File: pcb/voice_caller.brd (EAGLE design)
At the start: 52.4 x 59.1 mm, 44 parts, among them IC1 PRO_MICRO, IC2 LM386M-1, IC3 78L12SMD, K1 TQ2SA-L2-5V, U1 25F32006WSOI

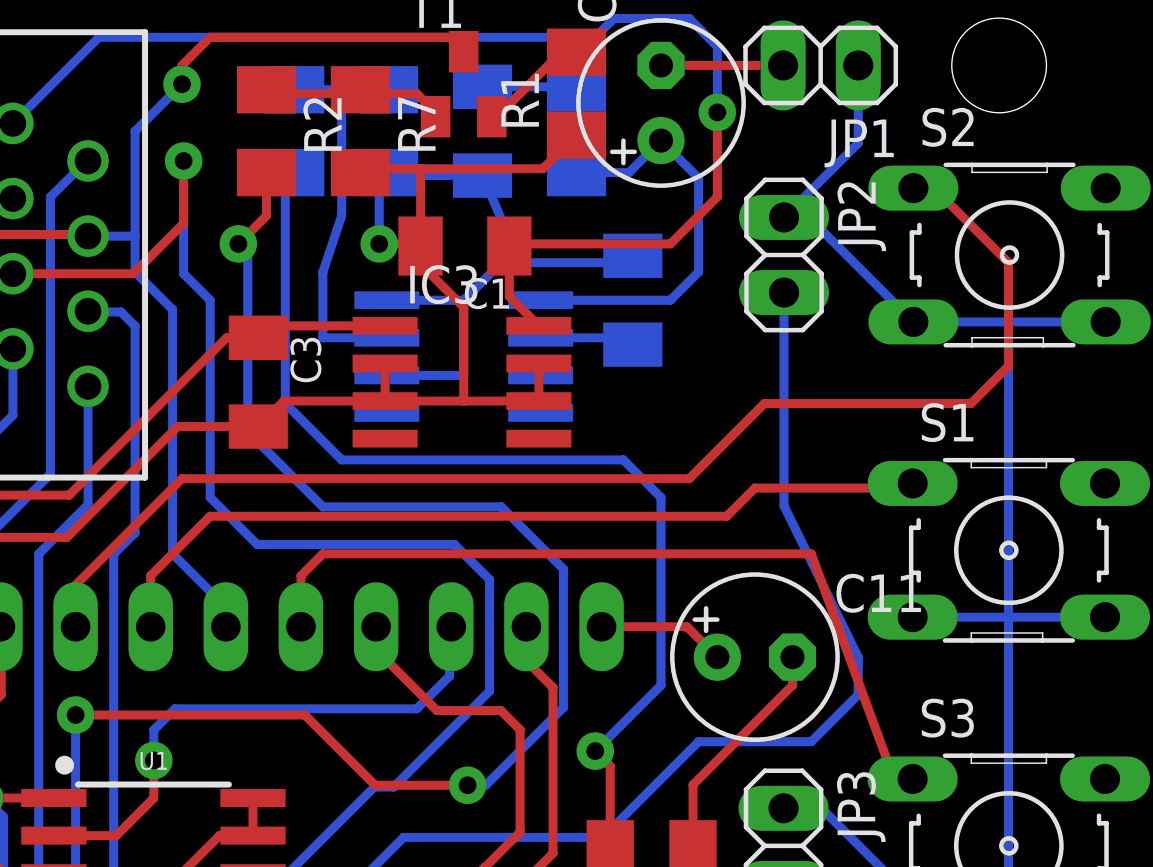
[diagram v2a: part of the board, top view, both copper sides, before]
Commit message: Bypass capacitor added for LM386.
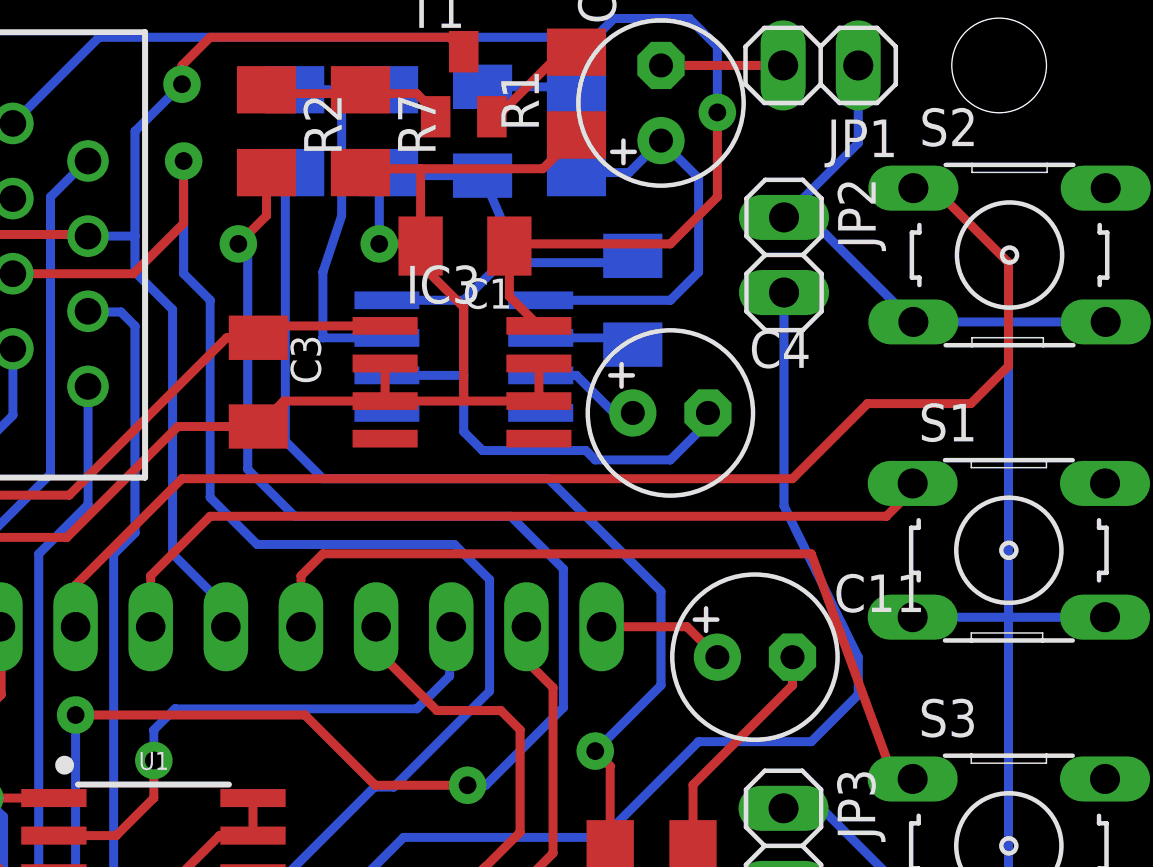
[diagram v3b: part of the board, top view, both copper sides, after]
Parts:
- added C4: (no value), rcl:E2,5-6
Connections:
- new net N$7: C4.+, IC2.7
- net GND: now also C4.-
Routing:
- net GND: track 301.6 -> 313.0 mm
- net N$7: track 0.00 -> 3.64 mm
- net AUDIO: track 49.1 -> 48.0 mm
- net PTT_SW: track 57.4 -> 58.1 mm
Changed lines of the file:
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@@
 <element name="R16" library="rcl" package="M1206" value="220" x="35.2425" y="59.3725" rot="MR90"/>
 <element name="C11" library="rcl" package="E2,5-6" value="" x="47.625" y="41.5925"/>
+<element name="C4" library="rcl" package="E2,5-6" value="" x="44.7675" y="49.8475"/>
 </elements>
 <signals>
@@
 <wire x1="35.2425" y1="57.9725" x2="34.925" y2="57.655" width="0.3048" layer="16"/>
 <wire x1="34.925" y1="57.655" x2="34.925" y2="55.5625" width="0.3048" layer="16"/>
+<contactref element="C4" pad="-"/>
+<wire x1="46.0375" y1="49.8475" x2="46.0375" y2="49.53" width="0.3048" layer="16"/>
+<wire x1="46.0375" y1="49.53" x2="44.7675" y2="48.26" width="0.3048" layer="16"/>
+<wire x1="44.7675" y1="48.26" x2="42.2275" y2="48.26" width="0.3048" layer="16"/>
+<wire x1="42.2275" y1="48.26" x2="41.91" y2="48.5775" width="0.3048" layer="16"/>
+<wire x1="41.91" y1="48.5775" x2="38.4175" y2="48.5775" width="0.3048" layer="16"/>
+<wire x1="38.4175" y1="48.5775" x2="37.7825" y2="49.2125" width="0.3048" layer="16"/>
+<wire x1="37.7825" y1="49.2125" x2="37.7825" y2="51.1175" width="0.3048" layer="16"/>
 </signal>
 <signal name="MOSI">
@@
 <wire x1="44.7675" y1="23.65375" x2="43.65625" y2="22.5425" width="0.3048" layer="1"/>
 <contactref element="R15" pad="2"/>
-<wire x1="43.18" y1="48.26" x2="44.45" y2="46.99" width="0.3048" layer="16"/>
-<wire x1="44.45" y1="46.99" x2="44.45" y2="40.64" width="0.3048" layer="16"/>
+<wire x1="40.64" y1="47.625" x2="44.45" y2="43.815" width="0.3048" layer="16"/>
+<wire x1="44.45" y1="43.815" x2="44.45" y2="40.64" width="0.3048" layer="16"/>
 <wire x1="44.45" y1="40.64" x2="42.2275" y2="38.4175" width="0.3048" layer="16"/>
 <via x="42.2275" y="38.4175" extent="1-16" drill="0.6" diameter="1.27" shape="square"/>
 <wire x1="42.2275" y1="38.4175" x2="42.7325" y2="37.9125" width="0.3048" layer="1"/>
 <wire x1="42.7325" y1="37.9125" x2="42.7325" y2="35.08375" width="0.3048" layer="1"/>
-<wire x1="43.18" y1="48.26" x2="33.655" y2="48.26" width="0.3048" layer="16"/>
-<wire x1="33.655" y1="48.26" x2="31.75" y2="50.165" width="0.3048" layer="16"/>
-<wire x1="31.75" y1="50.165" x2="31.75" y2="57.655" width="0.3048" layer="16"/>
+<wire x1="40.64" y1="47.625" x2="33.02" y2="47.625" width="0.3048" layer="16"/>
+<wire x1="33.02" y1="47.625" x2="31.75" y2="48.895" width="0.3048" layer="16"/>
+<wire x1="31.75" y1="48.895" x2="31.75" y2="57.655" width="0.3048" layer="16"/>
 <wire x1="31.75" y1="57.655" x2="32.0675" y2="57.9725" width="0.3048" layer="16"/>
 </signal>
@@
 <signal name="BUTTON2">
 <contactref element="S1" pad="1"/>
-<wire x1="29.21" y1="46.355" x2="46.6725" y2="46.355" width="0.3048" layer="1"/>
-<wire x1="46.6725" y1="46.355" x2="47.625" y2="47.3075" width="0.3048" layer="1"/>
-<wire x1="47.625" y1="47.3075" x2="52.800075" y2="47.3075" width="0.3048" layer="1"/>
+<wire x1="29.21" y1="46.355" x2="52.07" y2="46.355" width="0.3048" layer="1"/>
+<wire x1="52.07" y1="46.355" x2="53.0225" y2="47.3075" width="0.3048" layer="1"/>
+<wire x1="53.0225" y1="47.3075" x2="52.800075" y2="47.3075" width="0.3048" layer="1"/>
 <wire x1="52.800075" y1="47.3075" x2="52.95755" y2="47.464975" width="0.3048" layer="1"/>
 <contactref element="IC1" pad="19"/>
@@
 <signal name="BUTTON1">
 <contactref element="S2" pad="1"/>
-<wire x1="28.2575" y1="47.625" x2="45.4025" y2="47.625" width="0.3048" layer="1"/>
+<wire x1="28.2575" y1="47.625" x2="48.895" y2="47.625" width="0.3048" layer="1"/>
 <contactref element="IC1" pad="20"/>
 <wire x1="24.66" y1="42.62" x2="24.66" y2="44.0275" width="0.3048" layer="1"/>
 <wire x1="24.66" y1="44.0275" x2="28.2575" y2="47.625" width="0.3048" layer="1"/>
 <wire x1="52.9813" y1="57.5087" x2="52.9813" y2="57.446225" width="0.3048" layer="1"/>
-<wire x1="45.4025" y1="47.625" x2="47.9425" y2="50.165" width="0.3048" layer="1"/>
-<wire x1="47.9425" y1="50.165" x2="54.9275" y2="50.165" width="0.3048" layer="1"/>
+<wire x1="48.895" y1="47.625" x2="51.435" y2="50.165" width="0.3048" layer="1"/>
+<wire x1="51.435" y1="50.165" x2="54.9275" y2="50.165" width="0.3048" layer="1"/>
 <wire x1="54.9275" y1="50.165" x2="56.1975" y2="51.435" width="0.3048" layer="1"/>
 <wire x1="56.1975" y1="51.435" x2="56.1975" y2="54.9275" width="0.3048" layer="1"/>
@@
 <wire x1="34.7875" y1="37.2625" x2="32.4125" y2="39.6375" width="0.3048" layer="1"/>
 <wire x1="32.4125" y1="39.6375" x2="24.6625" y2="39.6375" width="0.3048" layer="1"/>
-<wire x1="41.15" y1="44.575" x2="39.0525" y2="46.6725" width="0.3048" layer="16"/>
-<wire x1="39.0525" y1="46.6725" x2="33.02" y2="46.6725" width="0.3048" layer="16"/>
-<wire x1="33.02" y1="46.6725" x2="30.48" y2="49.2125" width="0.3048" layer="16"/>
-<wire x1="30.48" y1="49.2125" x2="30.48" y2="55.245" width="0.3048" layer="16"/>
+<wire x1="41.15" y1="44.575" x2="39.37" y2="46.355" width="0.3048" layer="16"/>
+<wire x1="39.37" y1="46.355" x2="32.0675" y2="46.355" width="0.3048" layer="16"/>
+<wire x1="32.0675" y1="46.355" x2="30.48" y2="47.9425" width="0.3048" layer="16"/>
+<wire x1="30.48" y1="47.9425" x2="30.48" y2="55.245" width="0.3048" layer="16"/>
 <wire x1="30.48" y1="55.245" x2="30.1625" y2="55.5625" width="0.3048" layer="16"/>
 <via x="30.1625" y="55.5625" extent="1-16" drill="0.6" diameter="1.27" shape="square"/>
@@
 <wire x1="33.655" y1="56.515" x2="33.655" y2="60.7725" width="0.3048" layer="16"/>
 </signal>
+<signal name="N$7">
+<contactref element="C4" pad="+"/>
+<contactref element="IC2" pad="7"/>
+<wire x1="40.3825" y1="51.1175" x2="41.5925" y2="51.1175" width="0.3048" layer="16"/>
+<wire x1="41.5925" y1="51.1175" x2="42.8625" y2="49.8475" width="0.3048" layer="16"/>
+<wire x1="42.8625" y1="49.8475" x2="43.4975" y2="49.8475" width="0.3048" layer="16"/>
+</signal>
 </signals>

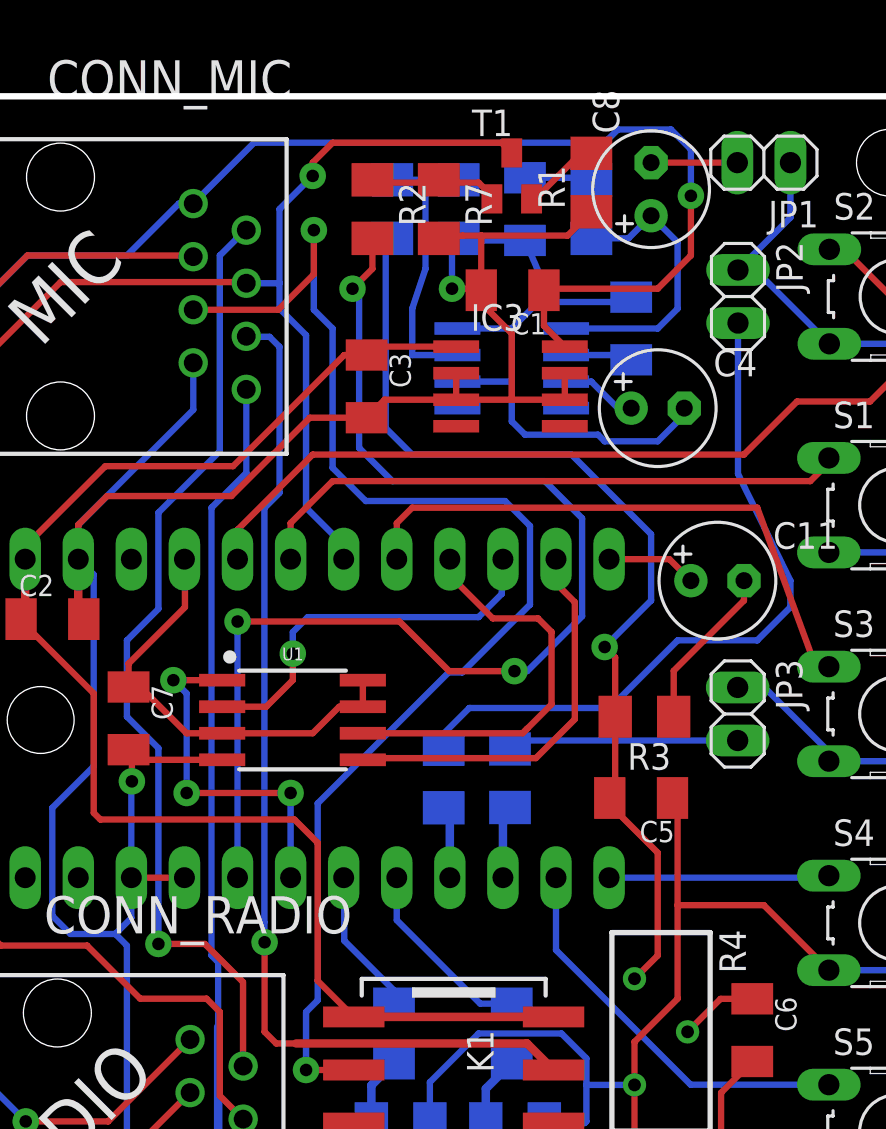
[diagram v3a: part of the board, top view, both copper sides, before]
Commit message: PTT sensing circuity added.
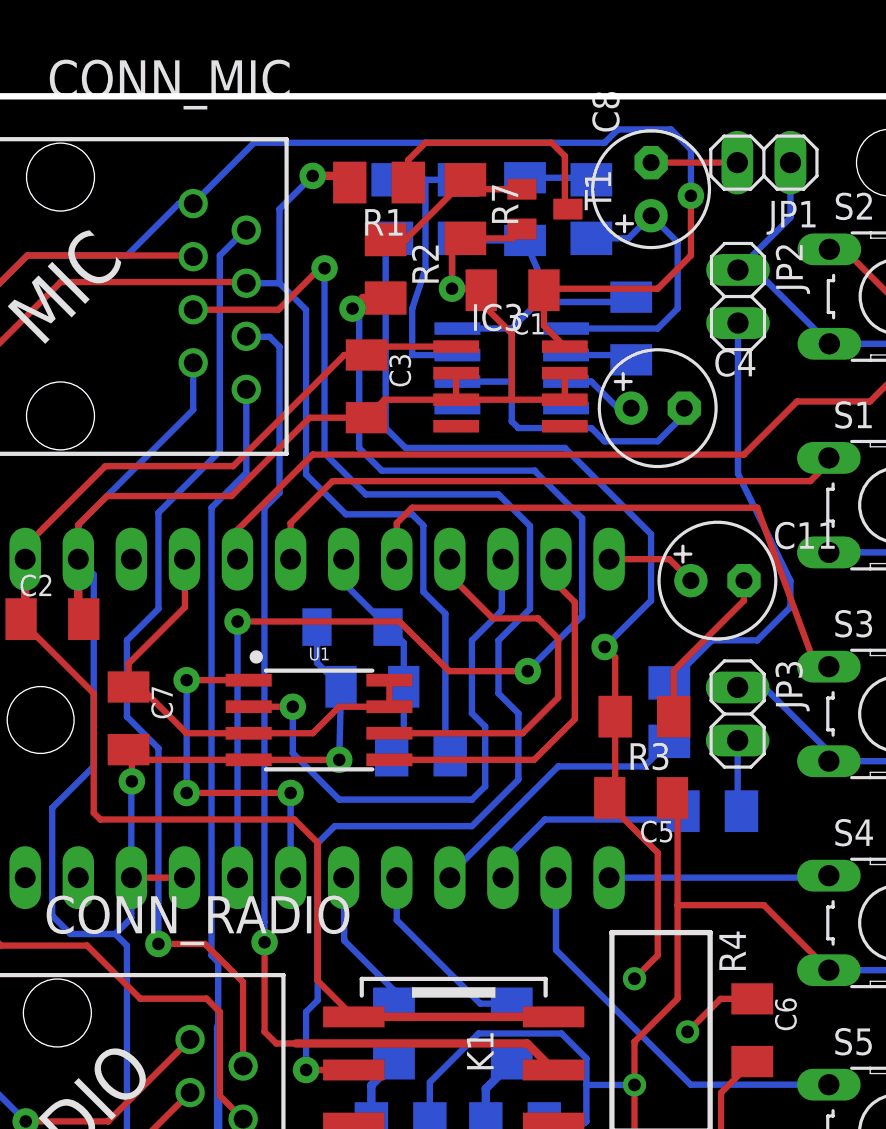
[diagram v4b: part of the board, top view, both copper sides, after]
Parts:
- added C12: 100nF, rcl:C1206K
- added D1: (no value), diode:SOD80C
- added R17: 10k, rcl:M1206
- moved R12 11.3 mm to (45.3, 35.3)
- moved R1 10.2 mm to (31.4, 60.6), turned to 180 degrees
- moved R13 9.80 mm to (47.4, 30.6), turned to 0 degrees
- moved R2 2.93 mm to (31.7, 56.5)
- moved T1 2.25 mm to (39.4, 59.4), turned to 270 degrees
- moved R7 1.27 mm to (35.6, 59.4)
- moved U1 1.27 mm to (28.6, 34.9)
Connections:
- new net N$8: R1.1, T1.C
- net GND: now also C12.1, D1.C, T1.E; no longer R1.1
- net PTT: now also R1.2, R17.2; no longer IC1.18, T1.C
- net PTT_SENSE: now also C12.2, D1.A, IC1.18, R17.1; no longer R1.2, T1.E
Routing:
- net N$4: track 34.0 -> 21.5 mm
- net N$8: track 0.00 -> 11.8 mm
- net N$12: track 3.64 -> 13.3 mm
- net MISO: track 18.6 -> 26.5 mm
- net GND: track 313.0 -> 320.6 mm, vias 4 -> 5
- net N$9: track 11.1 -> 3.46 mm
- net PTT_SENSE: track 3.76 -> 10.8 mm
- net N$15: track 3.70 -> 10.4 mm
- net PTT: track 92.4 -> 96.9 mm
- net PTT_SW: track 58.1 -> 56.2 mm
- net N$5: track 6.31 -> 7.89 mm
- net MOSI: track 19.4 -> 18.2 mm
- net +3V3: track 21.2 -> 22.4 mm
- net SCK: track 20.0 -> 18.8 mm
- net MIC_GND: track 64.1 -> 64.6 mm
